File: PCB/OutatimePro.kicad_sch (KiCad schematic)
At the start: 52 parts, among them IC1 PAM8904JPR, J1 USB_B_Micro_PCB_Edge_receptac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, J3 OSO_SWD, Q1 ALS-PT19-315C/L177/TR8, SW1 EVPAWED40, U1 ATSAML22N18A-CFUT, U2 MIC5365-3.3YMT, U3 USBLC6-2P6, U4 MAX40200ANS, U5 MAX40200ANS, U6 LIS2DW12TR, Y1 32.768kHz

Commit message: move mcu to part where it fits & add promotional artwork
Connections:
- net SEG39 is gone; now on net SEG29: LCD1.34 (SEG29)
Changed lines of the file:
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@@
 		)
 	)
-	(label "SEG39"
+	(label "SEG29"
 		(at 433.07 161.29 180)
 		(effects

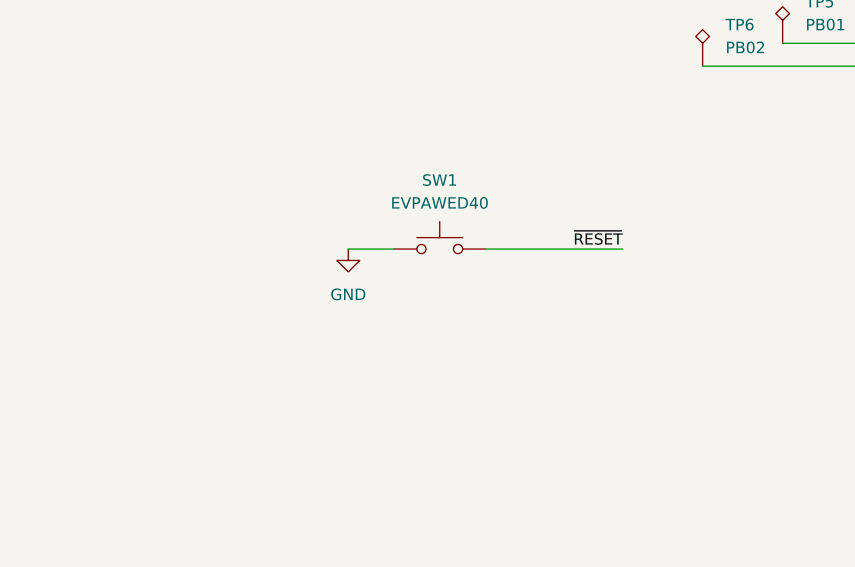
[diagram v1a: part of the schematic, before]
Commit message: add critical components for reliable operation (datasheet sch. checklist)
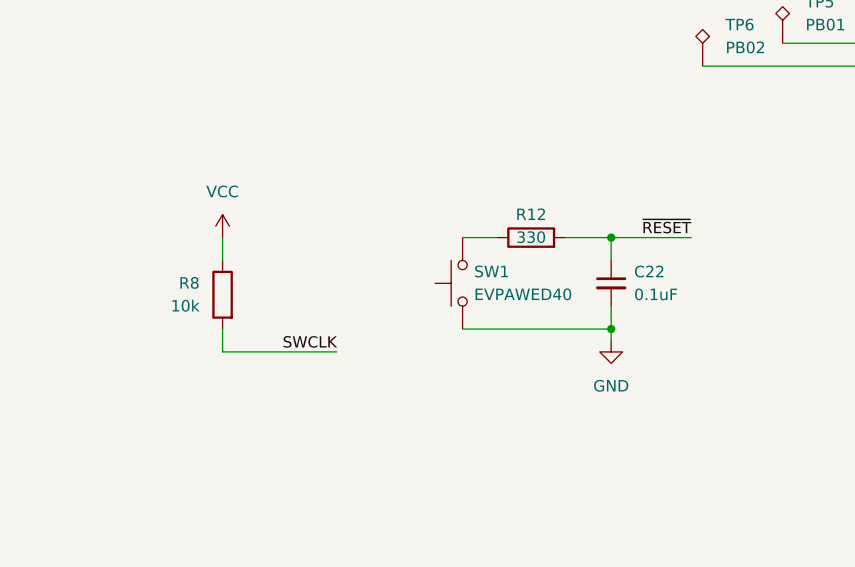
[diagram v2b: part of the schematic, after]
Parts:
- added C22: 0.1uF, Capacitor_SMD:C_0402_1005Metric, symbol Device:C_Small
- added R12: 330, Resistor_SMD:R_0402_1005Metric, symbol Device:R
- added R8: 10k, Resistor_SMD:R_0402_1005Metric, symbol Device:R
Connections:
- net BTN_ADJUST: now also R8.2
- net GND: now also C22.2
- net VCC: now also R8.1
- net ~{RESET}: now also C22.1, R12.2; no longer SW1.2
- new net: R12.1, SW1.2
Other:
- moved on the sheet: SW1

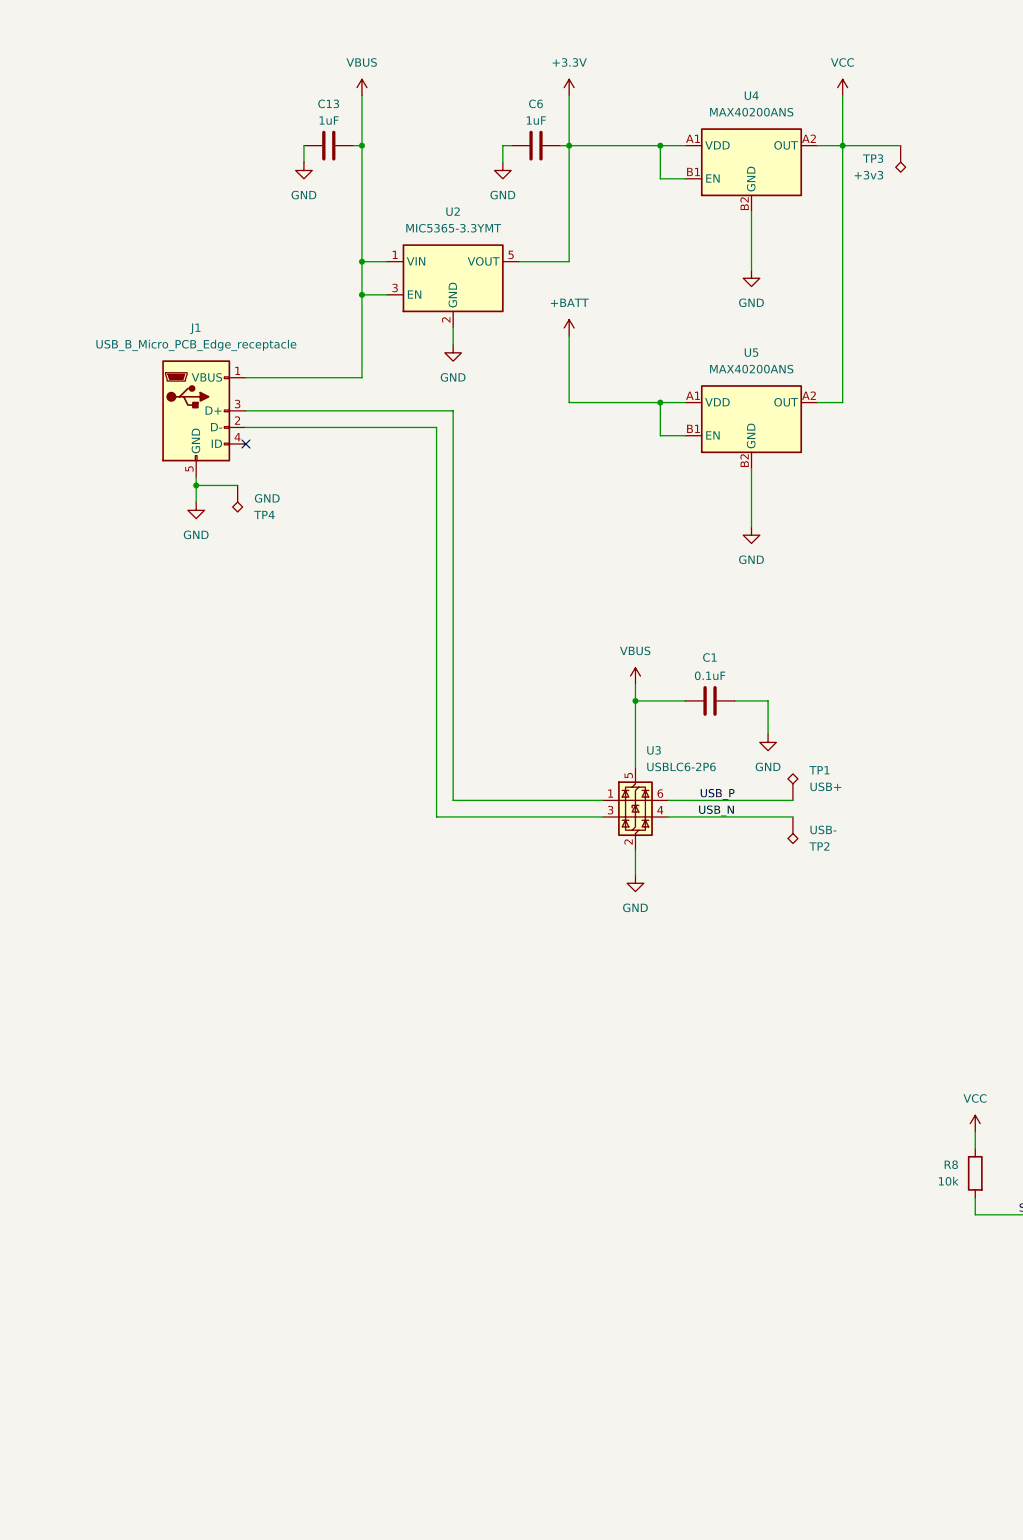
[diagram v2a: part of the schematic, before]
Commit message: Change programming header text size, change button pad copper size
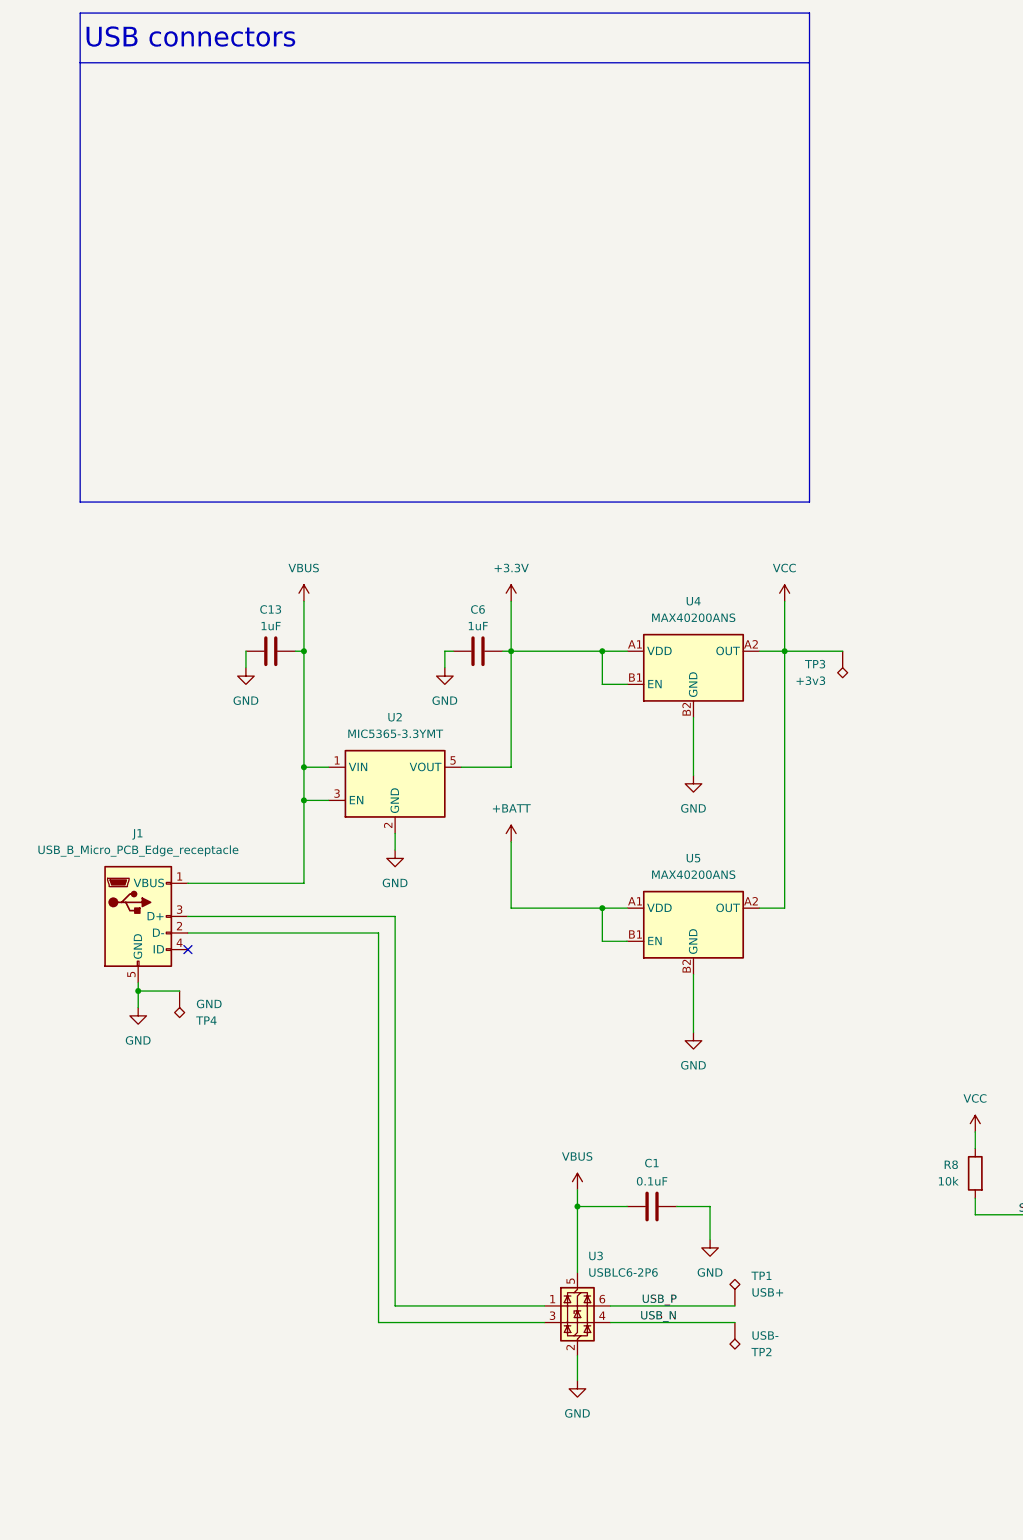
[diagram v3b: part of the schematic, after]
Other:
- note added: "USB connectors"
- moved on the sheet: C1, C13, C6, J1, TP1, TP2, TP3, TP4, U2, U3, U4, U5
